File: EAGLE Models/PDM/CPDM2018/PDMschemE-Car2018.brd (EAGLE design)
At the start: 85.1 x 102.9 mm, 45 parts, among them Q1 2N2907, Q2 2N2907, Q3 2N2907, Q4 2N2907, Q5 2N2907, Q6 2N2907

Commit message: Updated board with pinout for mcu power switch
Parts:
- removed U$3: A114898-ND, formula electric:A114898-ND
- added U$6: A30605-ND, formula electric:A30605-ND
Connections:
- removed net N$43: U$4.P$22
- new net MCU_POWER: U$4.P$22, U$6.P$4
- net FRONT/REAR_HARNESS: now also U$6.P$8
- net GND: now also U$6.P$1, U$6.P$2, U$6.P$3; no longer U$3.P$4, U$3.P$5, U$3.P$6
- net SBRIO/BMS/WIFI: now also U$6.P$5, U$6.P$6, U$6.P$7; no longer U$3.P$1, U$3.P$2, U$3.P$3
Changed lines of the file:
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@@
 <element name="U$7" library="diodes-inc" package="SOT23-3" value="MMBD4448H-7-F" x="-60.96" y="54.61"/>
 <element name="W.PUMPRELAY" library="panasonic" package="ACTP112" value="ACTP112ACTP112" x="-53.34" y="7.62"/>
-<element name="U$3" library="formula electric" package="A114898-ND" value="A114898-ND" x="13.97" y="88.9" locked="yes" rot="R90"/>
 <element name="U$4" library="TE" package="SUPERSEAL1.0_26POS_2ROW" value="SUPERSEAL1.0_26POS_2ROW" x="17.526" y="6.604" locked="yes"/>
+<element name="U$6" library="formula electric" package="A30605-ND" value="A30605-ND" x="-55.88" y="-21.59"/>
 </elements>
 <signals>
@@
 <contactref element="U$2" pad="P7"/>
 <contactref element="U$2" pad="P3"/>
-<contactref element="U$3" pad="P$4"/>
-<contactref element="U$3" pad="P$6"/>
-<contactref element="U$3" pad="P$5"/>
 <contactref element="U$4" pad="P$12"/>
 <contactref element="U$4" pad="P$13"/>
 <contactref element="U$4" pad="P$11"/>
+<contactref element="U$6" pad="P$1"/>
+<contactref element="U$6" pad="P$2"/>
+<contactref element="U$6" pad="P$3"/>
 <wire x1="55.88" y1="92.71" x2="58.42" y2="92.71" width="0" layer="19" extent="1-1"/>
-<wire x1="16.7259" y1="93.091" x2="55.88" y2="92.71" width="0" layer="19" extent="1-1"/>
-<wire x1="16.7259" y1="88.9" x2="16.7259" y2="93.091" width="0" layer="19" extent="1-1"/>
-<wire x1="16.7259" y1="84.709" x2="16.7259" y2="88.9" width="0" layer="19" extent="1-1"/>
-<wire x1="-13.818" y1="71.12" x2="16.7259" y2="84.709" width="0" layer="19" extent="1-1"/>
+<wire x1="-13.818" y1="71.12" x2="55.88" y2="92.71" width="0" layer="19" extent="1-1"/>
 <wire x1="-18.898" y1="71.12" x2="-13.818" y2="71.12" width="0" layer="19" extent="1-1"/>
 <wire x1="-23.978" y1="71.12" x2="-18.898" y2="71.12" width="0" layer="19" extent="1-1"/>
@@
 <wire x1="-47.8282" y1="6.9596" x2="-46.67" y2="53.51" width="0" layer="19" extent="1-1"/>
 <wire x1="-22.4282" y1="6.9596" x2="-47.8282" y2="6.9596" width="0" layer="19" extent="1-1"/>
+<wire x1="-53.7845" y1="-18.8341" x2="-47.8282" y2="6.9596" width="0" layer="19" extent="1-1"/>
+<wire x1="-57.9755" y1="-18.8341" x2="-53.7845" y2="-18.8341" width="0" layer="19" extent="1-1"/>
+<wire x1="-62.1665" y1="-18.8341" x2="-57.9755" y2="-18.8341" width="0" layer="19" extent="1-1"/>
 <wire x1="59.026" y1="6.604" x2="-22.4282" y2="6.9596" width="0" layer="19" extent="1-1"/>
 <wire x1="62.526" y1="6.604" x2="59.026" y2="6.604" width="0" layer="19" extent="1-1"/>
@@
 <contactref element="10AA" pad="1"/>
 <contactref element="10AA" pad="2"/>
-<contactref element="U$3" pad="P$1"/>
-<contactref element="U$3" pad="P$3"/>
-<contactref element="U$3" pad="P$2"/>
-<wire x1="11.2141" y1="88.9" x2="11.2141" y2="93.091" width="0" layer="19" extent="1-1"/>
-<wire x1="11.2141" y1="84.709" x2="11.2141" y2="88.9" width="0" layer="19" extent="1-1"/>
-<wire x1="-21.01" y1="76.2" x2="11.2141" y2="84.709" width="0" layer="19" extent="1-1"/>
-<wire x1="-26.543" y1="35.9918" x2="-21.01" y2="76.2" width="0" layer="19" extent="1-1"/>
-<wire x1="-26.543" y1="32.5882" x2="-26.543" y2="35.9918" width="0" layer="19" extent="1-1"/>
+<contactref element="U$6" pad="P$5"/>
+<contactref element="U$6" pad="P$6"/>
+<contactref element="U$6" pad="P$7"/>
+<wire x1="-57.9755" y1="-24.3459" x2="-62.1665" y2="-24.3459" width="0" layer="19" extent="1-1"/>
+<wire x1="-53.7845" y1="-24.3459" x2="-57.9755" y2="-24.3459" width="0" layer="19" extent="1-1"/>
+<wire x1="-26.543" y1="32.5882" x2="-53.7845" y2="-24.3459" width="0" layer="19" extent="1-1"/>
+<wire x1="-26.543" y1="35.9918" x2="-26.543" y2="32.5882" width="0" layer="19" extent="1-1"/>
+<wire x1="-21.01" y1="76.2" x2="-26.543" y2="35.9918" width="0" layer="19" extent="1-1"/>
 </signal>
 <signal name="BAT_BOX">
@@
 <contactref element="U$4" pad="P$20"/>
 <contactref element="U$4" pad="P$21"/>
-<wire x1="45.026" y1="9.604" x2="48.526" y2="9.604" width="0" layer="19" extent="1-1"/>
-<wire x1="-43.053" y1="32.5882" x2="45.026" y2="9.604" width="0" layer="19" extent="1-1"/>
+<contactref element="U$6" pad="P$8"/>
+<wire x1="-43.053" y1="32.5882" x2="-49.5935" y2="-24.3459" width="0" layer="19" extent="1-1"/>
 <wire x1="-43.053" y1="35.9918" x2="-43.053" y2="32.5882" width="0" layer="19" extent="1-1"/>
 <wire x1="-27.36" y1="76.2" x2="-43.053" y2="35.9918" width="0" layer="19" extent="1-1"/>
+<wire x1="45.026" y1="9.604" x2="-43.053" y2="32.5882" width="0" layer="19" extent="1-1"/>
+<wire x1="48.526" y1="9.604" x2="45.026" y2="9.604" width="0" layer="19" extent="1-1"/>
 </signal>
 <signal name="N$1">
@@
 <contactref element="U$4" pad="P$10"/>
 </signal>
-<signal name="N$43">
-<contactref element="U$4" pad="P$22"/>
-</signal>
 <signal name="N$44">
 <contactref element="U$4" pad="P$23"/>
@@
 <via x="8.128" y="76.2" extent="1-16" drill="3.302" diameter="5.08"/>
 </signal>
+<signal name="MCU_POWER">
+<contactref element="U$6" pad="P$4"/>
+<contactref element="U$4" pad="P$22"/>
+<wire x1="52.026" y1="9.604" x2="-49.5935" y2="-18.8341" width="0" layer="19" extent="1-1"/>
+</signal>
 </signals>

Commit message: placed connector on E-PDM
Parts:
- moved U$6 136.0 mm to (21.6, 90.2), turned to 90 degrees
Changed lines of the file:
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@@
 <element name="W.PUMPRELAY" library="panasonic" package="ACTP112" value="ACTP112ACTP112" x="-53.34" y="7.62"/>
 <element name="U$4" library="TE" package="SUPERSEAL1.0_26POS_2ROW" value="SUPERSEAL1.0_26POS_2ROW" x="17.526" y="6.604" locked="yes"/>
-<element name="U$6" library="formula electric" package="A30605-ND" value="A30605-ND" x="-55.88" y="-21.59"/>
+<element name="U$6" library="formula electric" package="A30605-ND" value="A30605-ND" x="21.59" y="90.17" rot="R90"/>
 </elements>
 <signals>
@@
 <wire x1="-47.8282" y1="6.9596" x2="-46.67" y2="53.51" width="0" layer="19" extent="1-1"/>
 <wire x1="-22.4282" y1="6.9596" x2="-47.8282" y2="6.9596" width="0" layer="19" extent="1-1"/>
-<wire x1="-53.7845" y1="-18.8341" x2="-47.8282" y2="6.9596" width="0" layer="19" extent="1-1"/>
-<wire x1="-57.9755" y1="-18.8341" x2="-53.7845" y2="-18.8341" width="0" layer="19" extent="1-1"/>
-<wire x1="-62.1665" y1="-18.8341" x2="-57.9755" y2="-18.8341" width="0" layer="19" extent="1-1"/>
+<wire x1="18.8341" y1="92.2655" x2="-47.8282" y2="6.9596" width="0" layer="19" extent="1-1"/>
+<wire x1="18.8341" y1="88.0745" x2="18.8341" y2="92.2655" width="0" layer="19" extent="1-1"/>
+<wire x1="18.8341" y1="83.8835" x2="18.8341" y2="88.0745" width="0" layer="19" extent="1-1"/>
 <wire x1="59.026" y1="6.604" x2="-22.4282" y2="6.9596" width="0" layer="19" extent="1-1"/>
 <wire x1="62.526" y1="6.604" x2="59.026" y2="6.604" width="0" layer="19" extent="1-1"/>
@@
 <contactref element="U$6" pad="P$6"/>
 <contactref element="U$6" pad="P$7"/>
-<wire x1="-57.9755" y1="-24.3459" x2="-62.1665" y2="-24.3459" width="0" layer="19" extent="1-1"/>
-<wire x1="-53.7845" y1="-24.3459" x2="-57.9755" y2="-24.3459" width="0" layer="19" extent="1-1"/>
-<wire x1="-26.543" y1="32.5882" x2="-53.7845" y2="-24.3459" width="0" layer="19" extent="1-1"/>
+<wire x1="24.3459" y1="88.0745" x2="24.3459" y2="83.8835" width="0" layer="19" extent="1-1"/>
+<wire x1="24.3459" y1="92.2655" x2="24.3459" y2="88.0745" width="0" layer="19" extent="1-1"/>
+<wire x1="-26.543" y1="32.5882" x2="24.3459" y2="92.2655" width="0" layer="19" extent="1-1"/>
 <wire x1="-26.543" y1="35.9918" x2="-26.543" y2="32.5882" width="0" layer="19" extent="1-1"/>
 <wire x1="-21.01" y1="76.2" x2="-26.543" y2="35.9918" width="0" layer="19" extent="1-1"/>
@@
 <contactref element="U$4" pad="P$21"/>
 <contactref element="U$6" pad="P$8"/>
-<wire x1="-43.053" y1="32.5882" x2="-49.5935" y2="-24.3459" width="0" layer="19" extent="1-1"/>
+<wire x1="-43.053" y1="32.5882" x2="24.3459" y2="96.4565" width="0" layer="19" extent="1-1"/>
 <wire x1="-43.053" y1="35.9918" x2="-43.053" y2="32.5882" width="0" layer="19" extent="1-1"/>
 <wire x1="-27.36" y1="76.2" x2="-43.053" y2="35.9918" width="0" layer="19" extent="1-1"/>
@@
 <contactref element="U$6" pad="P$4"/>
 <contactref element="U$4" pad="P$22"/>
-<wire x1="52.026" y1="9.604" x2="-49.5935" y2="-18.8341" width="0" layer="19" extent="1-1"/>
+<wire x1="52.026" y1="9.604" x2="18.8341" y2="96.4565" width="0" layer="19" extent="1-1"/>
 </signal>
 </signals>

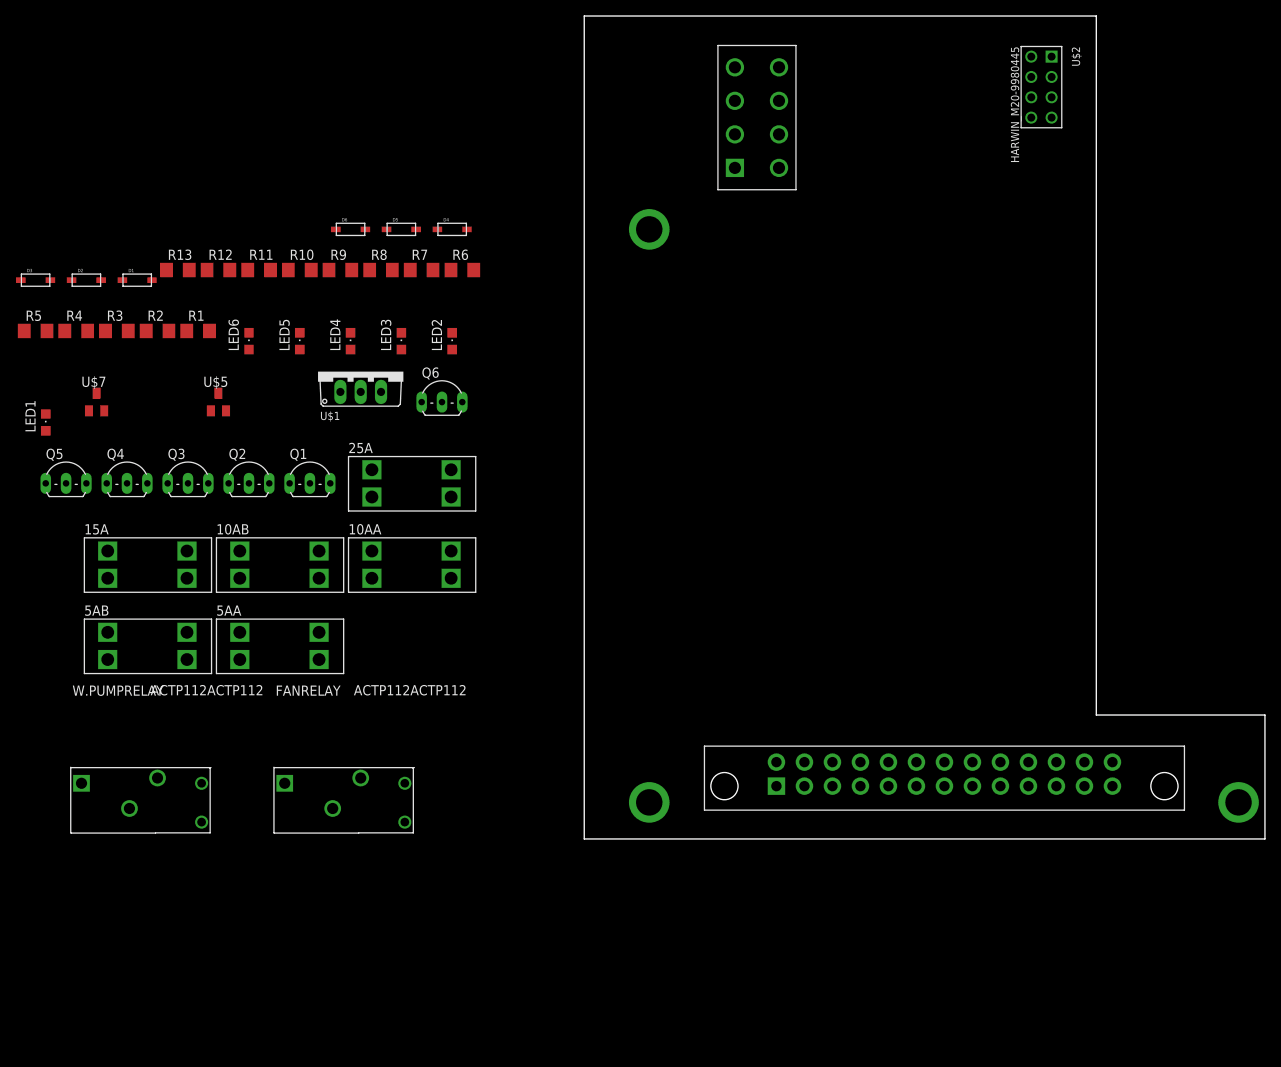
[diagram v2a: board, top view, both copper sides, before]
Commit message: Started board layout
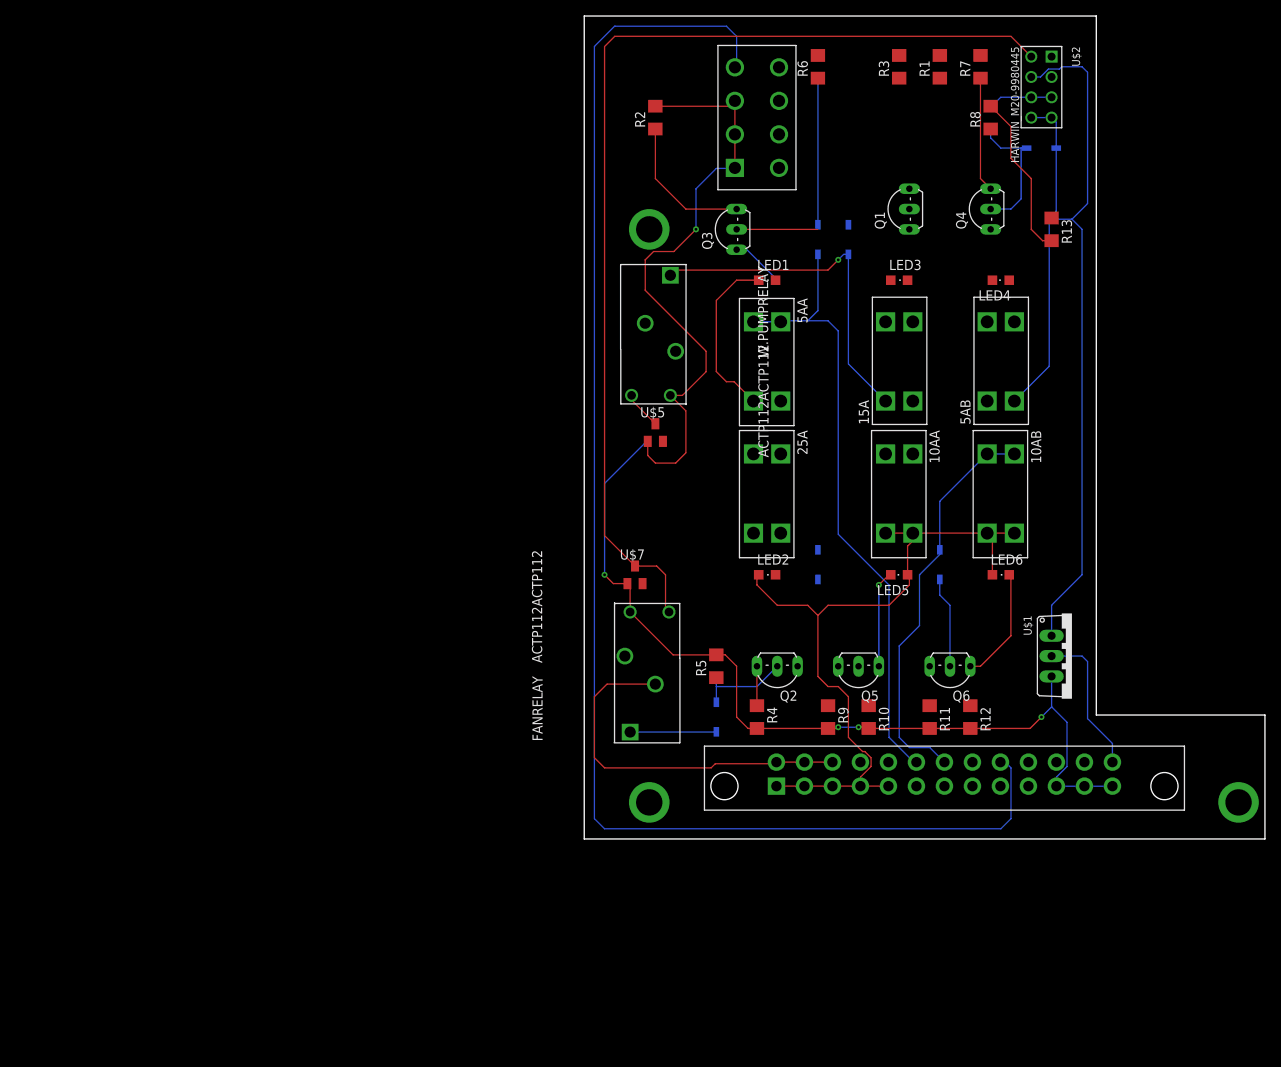
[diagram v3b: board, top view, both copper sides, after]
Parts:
- moved 5AB 112.5 mm to (52.1, 59.7), turned to 90 degrees
- moved Q4 111.7 mm to (49.5, 78.7), turned to 90 degrees
- moved R13 109.3 mm to (58.4, 76.2), turned to 270 degrees
- moved R12 109.3 mm to (48.3, 15.2), turned to 270 degrees
- moved R3 103.2 mm to (39.4, 96.5), turned to 90 degrees
- moved Q5 102.3 mm to (34.3, 20.3), turned to 180 degrees
- moved R11 100.7 mm to (43.2, 15.2), turned to 270 degrees
- moved R1 98.4 mm to (44.5, 96.5), turned to 90 degrees
- moved LED6 98.4 mm to (52.1, 33.0), turned to 270 degrees
- moved D3 97.9 mm to (29.2, 74.9), flipped to the bottom, turned to 270 degrees
- moved R4 97.8 mm to (21.6, 15.2), turned to 270 degrees
- moved 15A 97.4 mm to (39.4, 59.7), turned to 90 degrees
- moved D2 95.8 mm to (16.5, 15.2), flipped to the bottom, turned to 270 degrees
- moved R5 94.9 mm to (16.5, 21.6), turned to 90 degrees
- moved U$1 92.5 mm to (58.4, 22.9), turned to 270 degrees
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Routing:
- net GND: track 0.00 -> 215.9 mm, vias 0 -> 5
- net MCU_POWER: track 0.00 -> 180.9 mm
- net F.RELAY: track 0.00 -> 130.5 mm
- net 12V: track 0.00 -> 112.9 mm
- net FAN_PWM_IN: track 0.00 -> 83.7 mm
- net BAT_BOX: track 0.00 -> 78.1 mm
- net FRONT/REAR_HARNESS: track 0.00 -> 50.3 mm
- net FAN: track 0.00 -> 46.5 mm
- net N$10: track 0.00 -> 43.6 mm, vias 0 -> 1
- net DC/BSPD: track 0.00 -> 40.4 mm
- net N$14: track 0.00 -> 28.6 mm
- net FAN_PWM_OUT: track 0.00 -> 18.6 mm
- net N$2: track 0.00 -> 17.9 mm
- net N$18: track 0.00 -> 17.0 mm
- net N$27: track 0.00 -> 14.4 mm
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
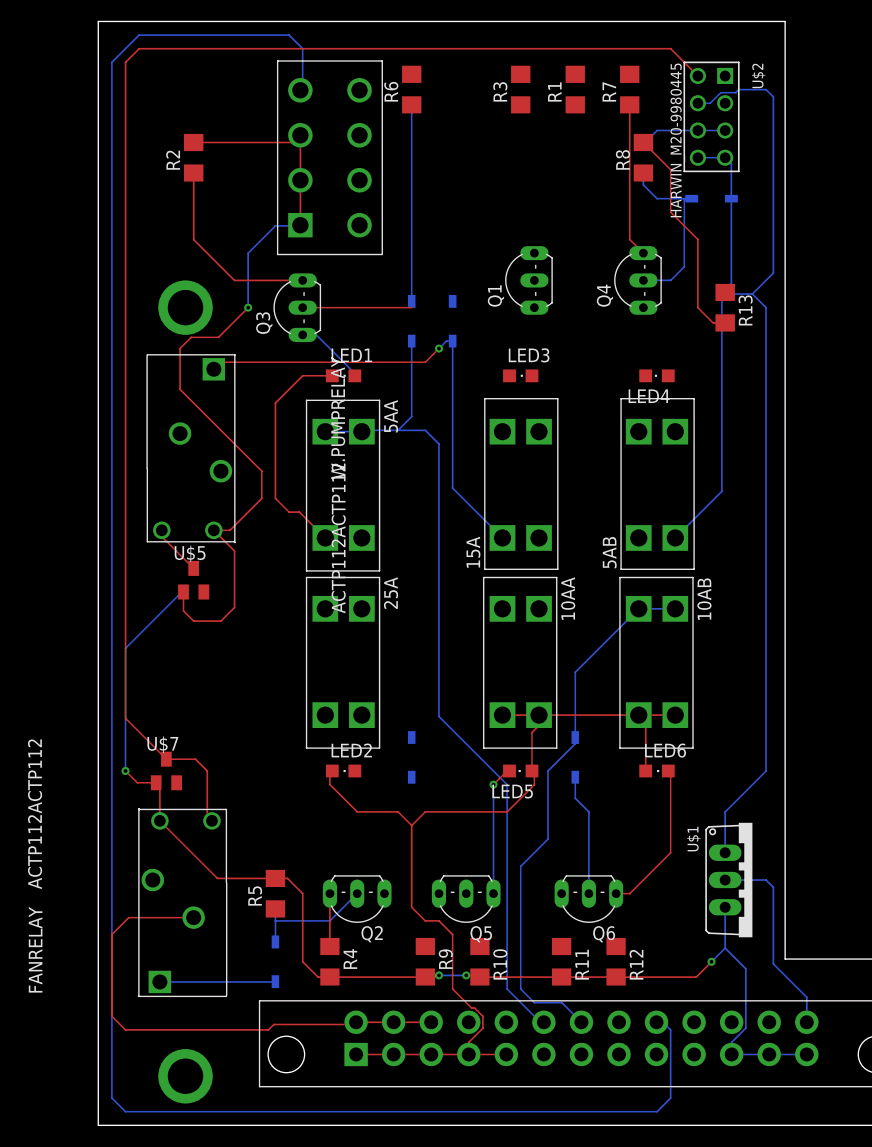
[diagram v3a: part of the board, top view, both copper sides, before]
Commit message: Board design
set up traces for high current
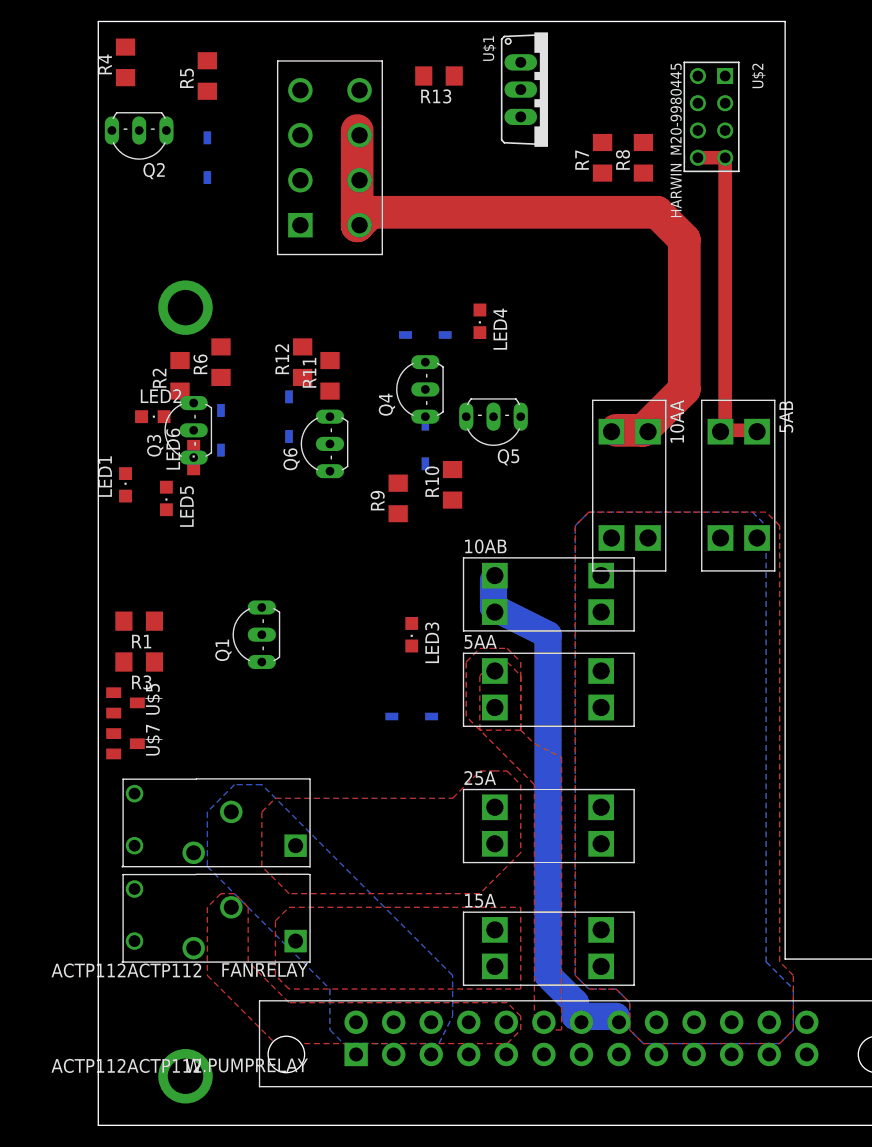
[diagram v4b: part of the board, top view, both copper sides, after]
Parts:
- moved R4 86.0 mm to (2.54, 99.1), turned to 90 degrees
- moved R5 76.5 mm to (10.2, 97.8)
- moved U$1 76.1 mm to (39.4, 96.5)
- moved D2 75.2 mm to (10.2, 90.2)
- moved Q2 74.0 mm to (3.81, 91.4)
- moved R3 64.1 mm to (3.81, 43.2), turned to 180 degrees
- moved R1 64.1 mm to (3.81, 47.0), turned to 180 degrees
- moved R12 63.1 mm to (19.1, 71.1), turned to 90 degrees
- moved R11 58.7 mm to (21.6, 69.8), turned to 90 degrees
- moved LED6 52.1 mm to (8.89, 62.2), turned to 0 degrees
- moved Q6 50.1 mm to (20.3, 63.5), turned to 90 degrees
- moved W.PUMPRELAY 44.5 mm to (8.89, 16.5), turned to 180 degrees
- moved Q5 44.5 mm to (36.8, 64.8)
- moved R10 44.5 mm to (33.0, 59.7), turned to 90 degrees
- moved R9 43.3 mm to (27.9, 58.4), turned to 90 degrees
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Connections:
- removed net N$21: U$4.P$6
- removed net N$44: U$4.P$23
- removed net N$45: U$4.P$24
- removed net N$46: U$4.P$25
- net 12V: now also U$4.P$22, U$4.P$23, U$4.P$24, U$4.P$25; no longer U$4.P$1, U$4.P$2, U$4.P$3, U$4.P$4, U$4.P$5
- net MCU_POWER: now also U$4.P$6; no longer U$4.P$22
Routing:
- net GND: track 215.9 -> 0.00 mm, vias 5 -> 0
- net MCU_POWER: track 180.9 -> 0.00 mm
- net F.RELAY: track 130.5 -> 0.00 mm
- net 12V: track 112.9 -> 0.00 mm
- net FAN_PWM_IN: track 83.7 -> 0.00 mm
- net BAT_BOX: track 78.1 -> 0.00 mm
- net SBRIO/BMS/WIFI: track 0.00 -> 62.8 mm
- net FAN: track 46.5 -> 0.00 mm
- net N$10: track 43.6 -> 0.00 mm, vias 1 -> 0
- net N$14: track 28.6 -> 0.00 mm
- net FAN_PWM_OUT: track 18.6 -> 0.00 mm
- net N$2: track 17.9 -> 0.00 mm
- net N$18: track 17.0 -> 0.00 mm
- net N$27: track 14.4 -> 0.00 mm
- net N$19: track 14.3 -> 0.00 mm
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- added copper zone on layer 1, net 12V
- added copper zone on layer 16, net 12V
- added copper zone on layer 1, net BAT_BOX
- added copper zone on layer 16, net FAN
- added copper zone on layer 1, net N$10
- added copper zone on layer 1, net N$4
- added copper zone on layer 1, net W.PUMP
